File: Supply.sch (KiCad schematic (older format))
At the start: 18 parts, among them U2 LM317_SOT223, U3 LM317_SOT223, U4 LM317_SOT223

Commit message: Layout
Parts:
- removed C17, C19, C21: 1µF, Capacitors_Tantalum_SMD:TantalC_SizeA_EIA-3216_HandSoldering, symbol CP
- added C31, C32, C33: 1µF, Capacitors_SMD:C_0805_HandSoldering, symbol C
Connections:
- net GND: now also C31.2, C32.2, C33.2
- net VCC: now also C31.1
- net VCC_AUX: now also C32.1
- net VCC_INT: now also C33.1
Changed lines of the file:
@@
 LIBS:switches
 LIBS:xo-14s
+LIBS:oscillator_xo
 LIBS:FPGABoard-cache
 EELAYER 25 0
@@
 $Descr A4 11693 8268
 encoding utf-8
-Sheet 3 5
+Sheet 5 5
 Title "Xilinx Spartan 3A Eval Board"
 Date "2016-07-15"
@@
 $EndComp
 $Comp
-L CP C19
-U 1 1 5748E1FE
-P 6950 2950
-F 0 "C19" H 6975 3050 50  0000 L CNN
-F 1 "1µF" H 6975 2850 50  0000 L CNN
-F 2 "Capacitors_Tantalum_SMD:TantalC_SizeA_EIA-3216_HandSoldering" H 6988 2800 50  0001 C CNN
-F 3 "" H 6950 2950 50  0000 C CNN
-	1    6950 2950
-	1    0    0    -1
-$EndComp
-$Comp
 L R R5
 U 1 1 5748E205
@@
 $EndComp
 $Comp
-L GND #PWR039
+L GND #PWR041
 U 1 1 5748E21A
 P 6100 3850
-F 0 "#PWR039" H 6100 3600 50  0001 C CNN
+F 0 "#PWR041" H 6100 3600 50  0001 C CNN
 F 1 "GND" H 6100 3700 50  0000 C CNN
 F 2 "" H 6100 3850 50  0000 C CNN
@@
 $EndComp
 $Comp
-L CP C21
-U 1 1 5748E22E
-P 8950 2950
-F 0 "C21" H 8975 3050 50  0000 L CNN
-F 1 "1µF" H 8975 2850 50  0000 L CNN
-F 2 "Capacitors_Tantalum_SMD:TantalC_SizeA_EIA-3216_HandSoldering" H 8988 2800 50  0001 C CNN
-F 3 "" H 8950 2950 50  0000 C CNN
-	1    8950 2950
-	1    0    0    -1
-$EndComp
-$Comp
-L GND #PWR040
+L GND #PWR042
 U 1 1 5748E235
 P 8000 3850
-F 0 "#PWR040" H 8000 3600 50  0001 C CNN
+F 0 "#PWR042" H 8000 3600 50  0001 C CNN
 F 1 "GND" H 8000 3700 50  0000 C CNN
 F 2 "" H 8000 3850 50  0000 C CNN
@@
 $EndComp
 $Comp
-L CP C17
-U 1 1 5748E250
-P 5050 2950
-F 0 "C17" H 5075 3050 50  0000 L CNN
-F 1 "1µF" H 5075 2850 50  0000 L CNN
-F 2 "Capacitors_Tantalum_SMD:TantalC_SizeA_EIA-3216_HandSoldering" H 5088 2800 50  0001 C CNN
-F 3 "" H 5050 2950 50  0000 C CNN
-	1    5050 2950
-	1    0    0    -1
-$EndComp
-$Comp
-L GND #PWR041
+L GND #PWR043
 U 1 1 5748E257
 P 4150 3850
-F 0 "#PWR041" H 4150 3600 50  0001 C CNN
+F 0 "#PWR043" H 4150 3600 50  0001 C CNN
 F 1 "GND" H 4150 3700 50  0000 C CNN
 F 2 "" H 4150 3850 50  0000 C CNN
@@
 $EndComp
 $Comp
-L GND #PWR042
+L GND #PWR044
 U 1 1 5748E266
 P 2700 3150
-F 0 "#PWR042" H 2700 2900 50  0001 C CNN
+F 0 "#PWR044" H 2700 2900 50  0001 C CNN
 F 1 "GND" H 2700 3000 50  0000 C CNN
 F 2 "" H 2700 3150 50  0000 C CNN
@@
 $EndComp
 $Comp
-L GND #PWR043
+L GND #PWR045
 U 1 1 5748E27A
 P 9550 3600
-F 0 "#PWR043" H 9550 3350 50  0001 C CNN
+F 0 "#PWR045" H 9550 3350 50  0001 C CNN
 F 1 "GND" H 9550 3450 50  0000 C CNN
 F 2 "" H 9550 3600 50  0000 C CNN
@@
 VCC_INT
 $Comp
-L VCC #PWR044
+L VCC #PWR046
 U 1 1 5786CA62
 P 5050 2250
-F 0 "#PWR044" H 5050 2100 50  0001 C CNN
+F 0 "#PWR046" H 5050 2100 50  0001 C CNN
 F 1 "VCC" H 5050 2400 50  0000 C CNN
 F 2 "" H 5050 2250 50  0000 C CNN
@@
 $EndComp
 $Comp
-L VCC #PWR045
+L VCC #PWR047
 U 1 1 5786CDE0
 P 9550 2650
-F 0 "#PWR045" H 9550 2500 50  0001 C CNN
+F 0 "#PWR047" H 9550 2500 50  0001 C CNN
 F 1 "VCC" H 9550 2800 50  0000 C CNN
 F 2 "" H 9550 2650 50  0000 C CNN
@@
 	1    0    0    -1
 $EndComp
+$Comp
+L C C31
+U 1 1 578EC0B1
+P 5050 2950
+F 0 "C31" H 5075 3050 50  0000 L CNN
+F 1 "1µF" H 5075 2850 50  0000 L CNN
+F 2 "Capacitors_SMD:C_0805_HandSoldering" H 5088 2800 50  0001 C CNN
+F 3 "" H 5050 2950 50  0000 C CNN
+	1    5050 2950
+	1    0    0    -1
+$EndComp
+$Comp
+L C C32
+U 1 1 578EC197
+P 6950 2950
+F 0 "C32" H 6975 3050 50  0000 L CNN
+F 1 "1µF" H 6975 2850 50  0000 L CNN
+F 2 "Capacitors_SMD:C_0805_HandSoldering" H 6988 2800 50  0001 C CNN
+F 3 "" H 6950 2950 50  0000 C CNN
+	1    6950 2950
+	1    0    0    -1
+$EndComp
+$Comp
+L C C33
+U 1 1 578EC21A
+P 8950 2950
+F 0 "C33" H 8975 3050 50  0000 L CNN
+F 1 "1µF" H 8975 2850 50  0000 L CNN
+F 2 "Capacitors_SMD:C_0805_HandSoldering" H 8988 2800 50  0001 C CNN
+F 3 "" H 8950 2950 50  0000 C CNN
+	1    8950 2950
+	1    0    0    -1
+$EndComp

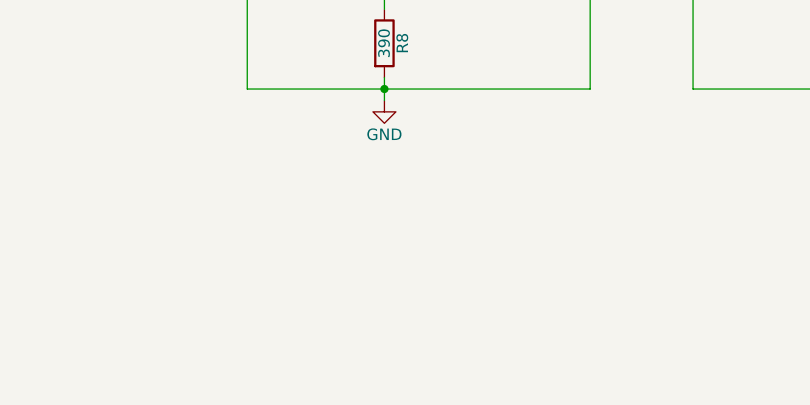
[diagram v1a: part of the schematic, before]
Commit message: Additional Caps at VCC, Layout
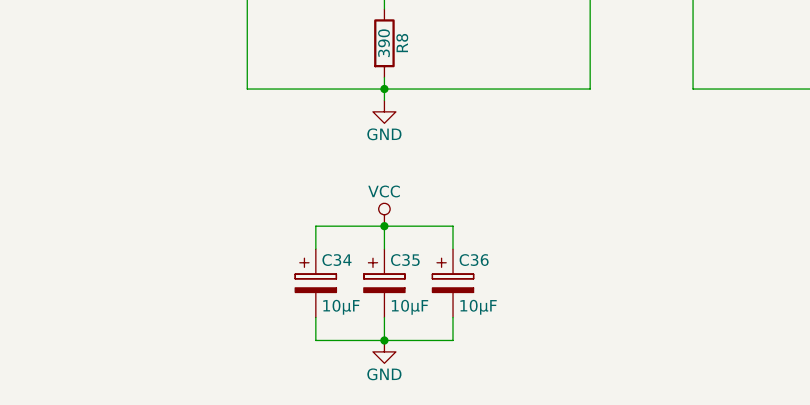
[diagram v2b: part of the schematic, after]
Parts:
- added C34, C35, C36: 10µF, Capacitors_SMD:c_elec_4x5.8, symbol CP
- C15: footprint Capacitors_SMD:c_elec_6.3x4.5 -> Capacitors_SMD:c_elec_4x5.8
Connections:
- net GND: now also C34.2, C35.2, C36.2
- net VCC: now also C34.1, C35.1, C36.1
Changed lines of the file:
@@
 F 0 "C15" H 2725 3050 50  0000 L CNN
 F 1 "10µF" H 2725 2850 50  0000 L CNN
-F 2 "Capacitors_SMD:c_elec_6.3x4.5" H 2738 2800 50  0001 C CNN
+F 2 "Capacitors_SMD:c_elec_4x5.8" H 2738 2800 50  0001 C CNN
 F 3 "" H 2700 2950 50  0000 C CNN
 	1    2700 2950
@@
 	1    0    0    -1
 $EndComp
+$Comp
+L CP C34
+U 1 1 57B0E3CD
+P 3850 4650
+F 0 "C34" H 3875 4750 50  0000 L CNN
+F 1 "10µF" H 3875 4550 50  0000 L CNN
+F 2 "Capacitors_SMD:c_elec_4x5.8" H 3888 4500 50  0001 C CNN
+F 3 "" H 3850 4650 50  0000 C CNN
+	1    3850 4650
+	1    0    0    -1
+$EndComp
+$Comp
+L CP C35
+U 1 1 57B0E6A2
+P 4150 4650
+F 0 "C35" H 4175 4750 50  0000 L CNN
+F 1 "10µF" H 4175 4550 50  0000 L CNN
+F 2 "Capacitors_SMD:c_elec_4x5.8" H 4188 4500 50  0001 C CNN
+F 3 "" H 4150 4650 50  0000 C CNN
+	1    4150 4650
+	1    0    0    -1
+$EndComp
+$Comp
+L CP C36
+U 1 1 57B0E6F6
+P 4450 4650
+F 0 "C36" H 4475 4750 50  0000 L CNN
+F 1 "10µF" H 4475 4550 50  0000 L CNN
+F 2 "Capacitors_SMD:c_elec_4x5.8" H 4488 4500 50  0001 C CNN
+F 3 "" H 4450 4650 50  0000 C CNN
+	1    4450 4650
+	1    0    0    -1
+$EndComp
+$Comp
+L VCC #PWR048
+U 1 1 57B0E751
+P 4150 4400
+F 0 "#PWR048" H 4150 4250 50  0001 C CNN
+F 1 "VCC" H 4150 4550 50  0000 C CNN
+F 2 "" H 4150 4400 50  0000 C CNN
+F 3 "" H 4150 4400 50  0000 C CNN
+	1    4150 4400
+	1    0    0    -1
+$EndComp
+$Comp
+L GND #PWR049
+U 1 1 57B0E8D6
+P 4150 4900
+F 0 "#PWR049" H 4150 4650 50  0001 C CNN
+F 1 "GND" H 4150 4750 50  0000 C CNN
+F 2 "" H 4150 4900 50  0000 C CNN
+F 3 "" H 4150 4900 50  0000 C CNN
+	1    4150 4900
+	1    0    0    -1
+$EndComp
+Wire Wire Line
+	3850 4400 4450 4400
+Wire Wire Line
+	3850 4400 3850 4500
+Wire Wire Line
+	4450 4400 4450 4500
+Connection ~ 4150 4400
+Wire Wire Line
+	4150 4500 4150 4400
+Wire Wire Line
+	3850 4800 3850 4900
+Wire Wire Line
+	3850 4900 4450 4900
+Wire Wire Line
+	4450 4900 4450 4800
+Connection ~ 4150 4900
+Wire Wire Line
+	4150 4800 4150 4900
 $EndSCHEMATC

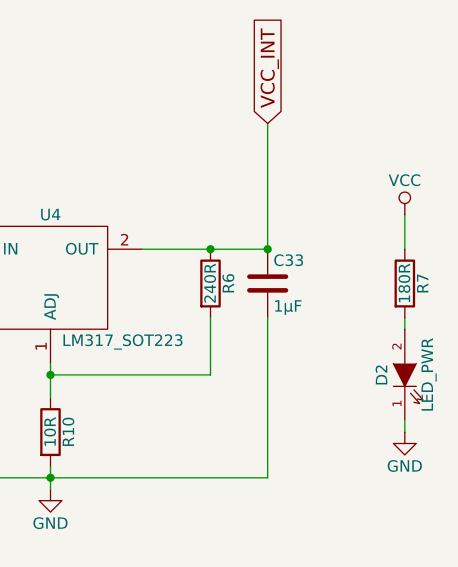
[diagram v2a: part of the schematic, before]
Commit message: All Resistors 0805, New Buttons
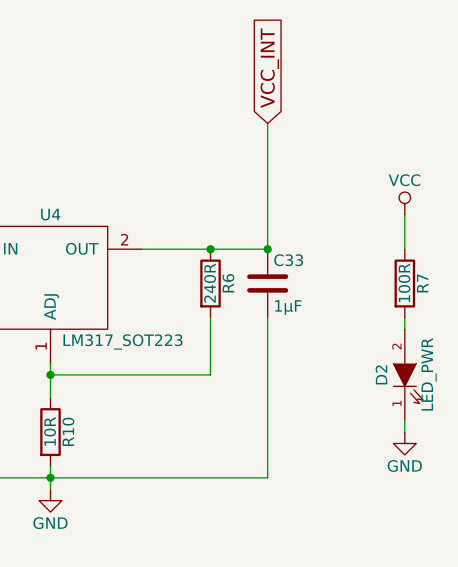
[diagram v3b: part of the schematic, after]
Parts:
- R7: value 180R -> 100R
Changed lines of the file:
@@
 P 9550 2950
 F 0 "R7" V 9630 2950 50  0000 C CNN
-F 1 "180R" V 9550 2950 50  0000 C CNN
+F 1 "100R" V 9550 2950 50  0000 C CNN
 F 2 "Resistors_SMD:R_0805_HandSoldering" V 9480 2950 50  0001 C CNN
 F 3 "" H 9550 2950 50  0000 C CNN

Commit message: Ready for Production
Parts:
- added C37, C38, C39: 10µF, Capacitors_SMD:C_0805_HandSoldering, symbol C
- added D8, D9: ES1DL, w_smd_diode:sod323, symbol D
- D2: value LED_PWR -> Green; symbol LED -> LED-RESCUE-FPGABoard
- R10: value 10R -> 1R
- R7: value 100R -> 36R
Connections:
- net GND: now also C37.2, C38.2, C39.2
- net VCC: now also D8.2 (A), D9.1 (K); no longer C18.1, U3.3 (IN)
- net V_USB: now also C18.1, U3.3 (IN), D8.1 (K)
- net at R5.2, R9.1, U3.1 (ADJ): now also C38.1
- net at R10.1, R6.2, U4.1 (ADJ): now also C39.1
- net at R4.2, R8.1, U2.1 (ADJ): now also C37.1, D9.2 (A)
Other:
- note added: "1,26V"
- note added: "3,3V"
- note added: "Evtl noch 1µ Tantal"
- moved on the sheet: C15, C16, C18, C20, C31, C32, C33, C34, C35, C36, D2, R10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

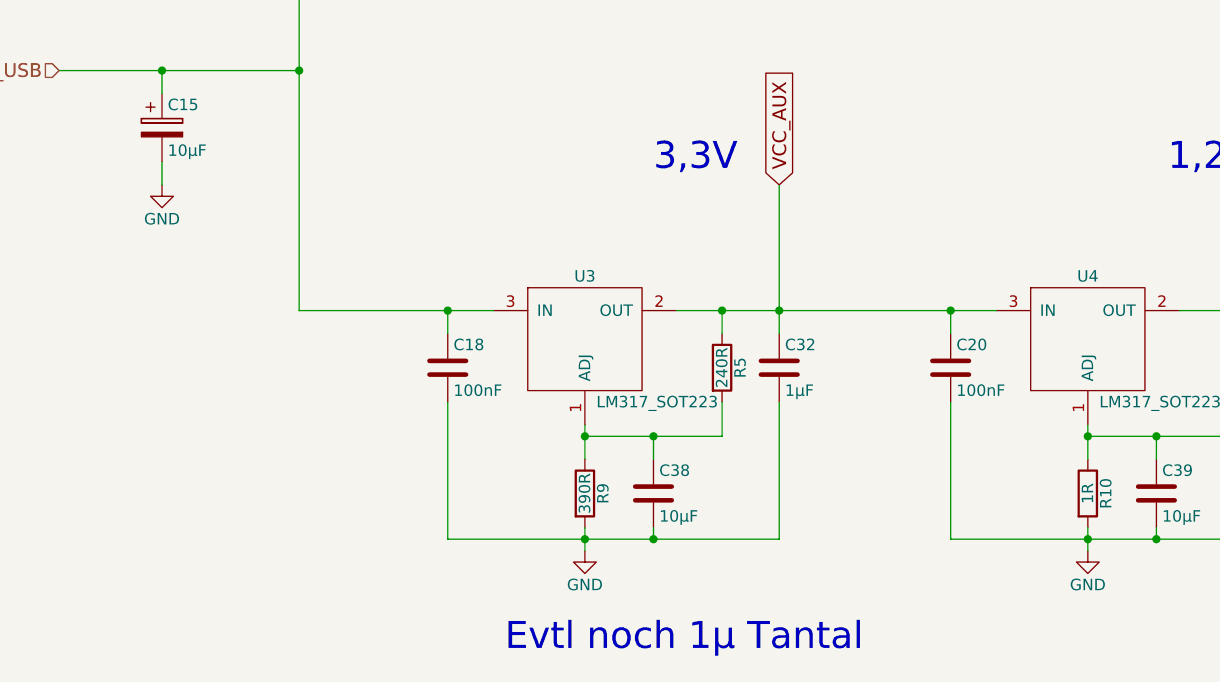
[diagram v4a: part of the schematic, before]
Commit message: Changed SPI Connection to support Multi-Master
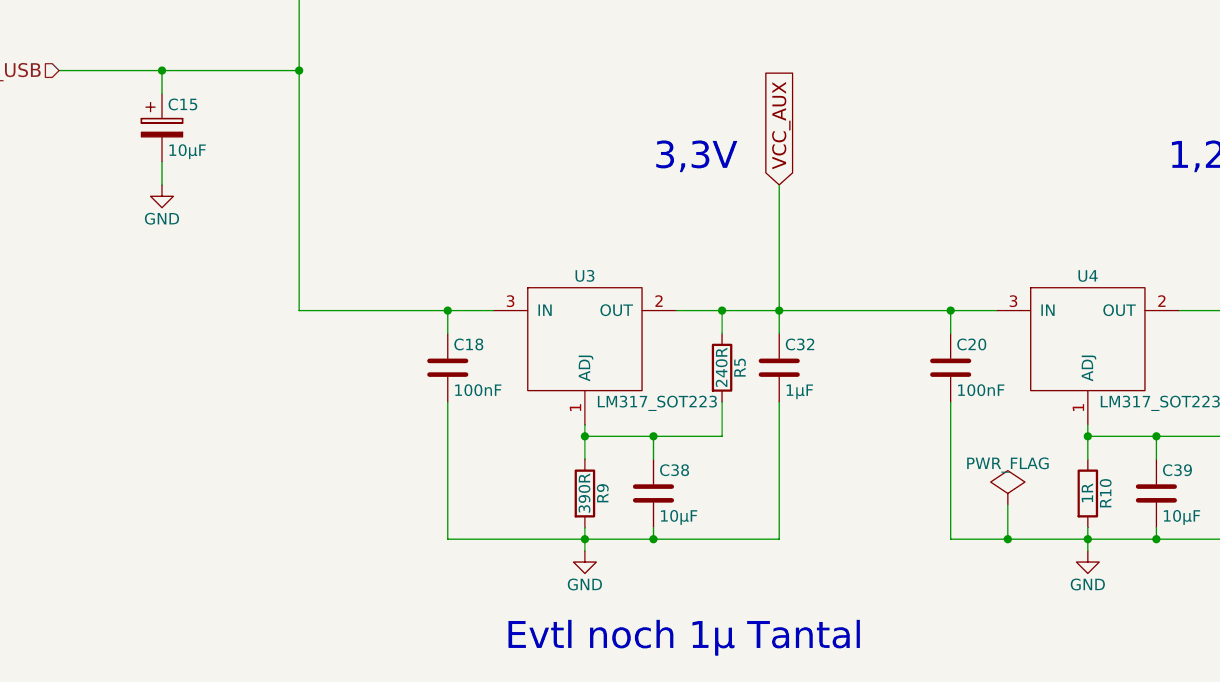
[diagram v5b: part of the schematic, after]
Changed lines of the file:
@@
 $EndComp
 $Comp
-L GND #PWR030
+L GND #PWR036
 U 1 1 5748E21A
 P 5300 5450
-F 0 "#PWR030" H 5300 5200 50  0001 C CNN
+F 0 "#PWR036" H 5300 5200 50  0001 C CNN
 F 1 "GND" H 5300 5300 50  0000 C CNN
 F 2 "" H 5300 5450 50  0000 C CNN
@@
 $EndComp
 $Comp
-L GND #PWR031
+L GND #PWR037
 U 1 1 5748E235
 P 7500 5450
-F 0 "#PWR031" H 7500 5200 50  0001 C CNN
+F 0 "#PWR037" H 7500 5200 50  0001 C CNN
 F 1 "GND" H 7500 5300 50  0000 C CNN
 F 2 "" H 7500 5450 50  0000 C CNN
@@
 $EndComp
 $Comp
-L GND #PWR032
+L GND #PWR038
 U 1 1 5748E257
 P 5250 2800
-F 0 "#PWR032" H 5250 2550 50  0001 C CNN
+F 0 "#PWR038" H 5250 2550 50  0001 C CNN
 F 1 "GND" H 5250 2650 50  0000 C CNN
 F 2 "" H 5250 2800 50  0000 C CNN
@@
 $EndComp
 $Comp
-L GND #PWR033
+L GND #PWR039
 U 1 1 5748E266
 P 3450 3850
-F 0 "#PWR033" H 3450 3600 50  0001 C CNN
+F 0 "#PWR039" H 3450 3600 50  0001 C CNN
 F 1 "GND" H 3450 3700 50  0000 C CNN
 F 2 "" H 3450 3850 50  0000 C CNN
@@
 	6500 1200 6500 1850
 Wire Wire Line
-	3450 3750 3450 3850
-Wire Wire Line
 	7500 5350 7500 5450
 Wire Wire Line
@@
 VCC_INT
 $Comp
-L VCC #PWR034
+L VCC #PWR040
 U 1 1 5786CA62
 P 6500 1200
-F 0 "#PWR034" H 6500 1050 50  0001 C CNN
+F 0 "#PWR040" H 6500 1050 50  0001 C CNN
 F 1 "VCC" H 6500 1350 50  0000 C CNN
 F 2 "" H 6500 1200 50  0000 C CNN
@@
 $EndComp
 $Comp
-L VCC #PWR035
+L VCC #PWR041
 U 1 1 57B0E751
 P 8450 1950
-F 0 "#PWR035" H 8450 1800 50  0001 C CNN
+F 0 "#PWR041" H 8450 1800 50  0001 C CNN
 F 1 "VCC" H 8450 2100 50  0000 C CNN
 F 2 "" H 8450 1950 50  0000 C CNN
@@
 $EndComp
 $Comp
-L GND #PWR036
+L GND #PWR042
 U 1 1 57B0E8D6
 P 8450 2450
-F 0 "#PWR036" H 8450 2200 50  0001 C CNN
+F 0 "#PWR042" H 8450 2200 50  0001 C CNN
 F 1 "GND" H 8450 2300 50  0000 C CNN
 F 2 "" H 8450 2450 50  0000 C CNN
@@
 	5650 1750 6950 1750
 Connection ~ 6500 1750
+Wire Wire Line
+	3450 3850 3450 3750
+$Comp
+L PWR_FLAG #FLG043
+U 1 1 58BB3CF3
+P 7150 5250
+F 0 "#FLG043" H 7150 5345 50  0001 C CNN
+F 1 "PWR_FLAG" H 7150 5430 50  0000 C CNN
+F 2 "" H 7150 5250 50  0000 C CNN
+F 3 "" H 7150 5250 50  0000 C CNN
+	1    7150 5250
+	1    0    0    -1
+$EndComp
+Wire Wire Line
+	7150 5250 7150 5400
+Connection ~ 7150 5400
 $EndSCHEMATC
